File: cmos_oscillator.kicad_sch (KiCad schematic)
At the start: 5 parts, among them X1 YC24.576MUBCE2O

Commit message: Fixed a lot more mistakes...
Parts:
- X1: value YC24.576MUBCE2O -> SG-8018CE 30.720000MHz TJHPA; Price (none) -> $0.81
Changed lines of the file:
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@@
 			)
 		)
-		(property "Value" "YC24.576MUBCE2O"
+		(property "Value" "SG-8018CE 30.720000MHz TJHPA"
 			(at 123.19 87.5598 0)
 			(hide yes)
@@
 			)
 		)
-		(property "Datasheet" "https://jlc-prod-smt.oss-eu-central-1.aliyuncs.com/smtDataManualFile/8588933966032617472-C390505.pdf?response-content-disposition=attachment%3B%20filename%3DC390505.pdf%3B%20filename%2A%3DUTF-8%27%27C390505.pdf&x-oss-date=20260713T192353Z&x-oss-expires=1800&x-oss-security-token=CAISgAN1q6Ft5B2yfSjIr5vDP9Dej5xk%2BpGdWEveplljb850orDClzz2IHhMdHJsAOodtv0%2FmmhT6PkclqRLcbhpcmfjV%2BZHzLB8qeYbqwhc4J7b16cNrbH4M4H6aXeirtuwDsz9SNTCALjPD3nPii50x5bjaDymRCbLGJaViJlhHLN1Ow6jdmhpCctxLAlvo9NgFxm3D%2Fu2NQPwiWf9FVdhvhEG6Vly8qOi2MaRmFy8yFTx0b0SvJ%2BjYMrmPctoN9JnSdC5mfdzau3a1TJ84gRD0a5wkaVA1zbDs5bfISEIuUzebreLqY03dV4mOvdqIcMe8qigz88fk%2FfIioH6xyxKOexoSCnFTOiiupCcQLPyao9jLu6iayqViY7QaIOTqQohZmkAMwVOasAsI3Ngh4zF97Qt0cVNkXO9gWfLI8DtuMleWhqAVs9ZwtHD0eS19jklBdzSlusJRAJJUVBflCeKEaRNSAd3WGhEfM2%2BBt4QT30w5N2u00S8OSMIzW17T6KWD5sagAEH0XQONBvK6BPLgnV8C207PLCKWk33RIXe%2FHW%2F%2BZhfMTLPa0UGk%2FYzlRC4zZHvrydpEGvZPRvOS0gXofU%2F2USkHG86fPOzGUhEgAFDSFwfe%2FrWC2%2FtY7pQNlxUNhLS%2BtO77iZMJH7wIZrwCswWjOwBqQYZ0YqcFTXTkg419%2FMEByAA&x-oss-signature-version=OSS4-HMAC-SHA256&x-oss-credential=STS.NXvtjjbCEMSvZmoBY6cAXMuiu%2F20260713%2Feu-central-1%2Foss%2Faliyun_v4_request&x-oss-signature=465519691e5ea808d0ae9e849a0f4727078b0ea6ca732cde5a2652c1c89228d5"
+		(property "Datasheet" "https://jlc-prod-smt.oss-eu-central-1.aliyuncs.com/smtDataManualFile/8588933966032617472-C390505.pdf?response-content-disposition=attachment%3B%20filename%3DC390505.pdf%3B%20filename%2A%3DUTF-8%27%27C390505.pdf&x-oss-date=20260722T003906Z&x-oss-expires=1800&x-oss-security-token=CAISgAN1q6Ft5B2yfSjIr5rHM%2B3smZ1Gx5CjaXPhtkIPXbwVnITJkTz2IHhMdHJsAOodtv0%2FmmhT6PkclqRLcbhpcmfjV%2BZHzLB8qeAV7l5R4J7b16cNrbH4M4H6aXeirtuwDsz9SNTCALjPD3nPii50x5bjaDymRCbLGJaViJlhHLN1Ow6jdmhpCctxLAlvo9NgFxm3D%2Fu2NQPwiWf9FVdhvhEG6Vly8qOi2MaRmFy8yFTx0b0SvJ%2BjYMrmPctoN9JnSdC5mfdzau3a1TJ84gRD0a5wkaVA1zbDs5bfISEIuUzebreLqY03dV4mOvdqIcMe8qigz88fk%2FfIioH6xyxKOexoSCnFTOiiupCcQLPyao9jLu6iayqViY7QaIOTqQohZmkAMwVOasAsI3Ngh4zF97Qt0cVNkXO9gWfLI8DtuMleWhpDE1NnmtHD0eS19jklBdzSlusJRAJJUVBflCeKEaRNSAd3WGhEfM2%2BBt4QT30w5N2u00S8OSMIMiDpfqKWD5sagAEIuex4%2FS4WddUM%2Fq31QMVuF1DjmKritBzmY7UsaeVXE5Y6cA2DIdCzyPbeZ7RXLbCbbvJ2w5S1gitzOQ2fpNn9WVrjqKde8H8UphDH%2FgQAWjP3Pk81SE5E2wJntjGHD%2B6K7yM2tP4pwvLZeXjm3G7dh4KBqQB8jh4W0%2FJBLiEqkiAA&x-oss-signature-version=OSS4-HMAC-SHA256&x-oss-credential=STS.NYrxWXtBgpRHkUPRBZQ39sAbs%2F20260722%2Feu-central-1%2Foss%2Faliyun_v4_request&x-oss-signature=a025f17aa42fdaad05dfb79b8c5d52c1bd33945fd76a011e5d9cb6ae45cacf93"
 			(at 107.95 91.44 0)
 			(hide yes)
@@
 			)
 		)
-		(property "Description" "SG-8018CE 30.720000MHz TJHPA"
+		(property "Description" "-40℃~+105℃ 1.8V~3.3V 30.72MHz ±50ppm SMD3225-4P Programmable Oscillators ROHS"
 			(at 110.49 91.44 0)
 			(hide yes)
@@
 			(at 110.49 91.44 0)
 			(hide yes)
+			(show_name no)
+			(do_not_autoplace no)
+			(effects
+				(font
+					(size 1.27 1.27)
+				)
+			)
+		)
+		(property "Price" "$0.81"
+			(at 110.49 91.44 0)
+			(hide yes)

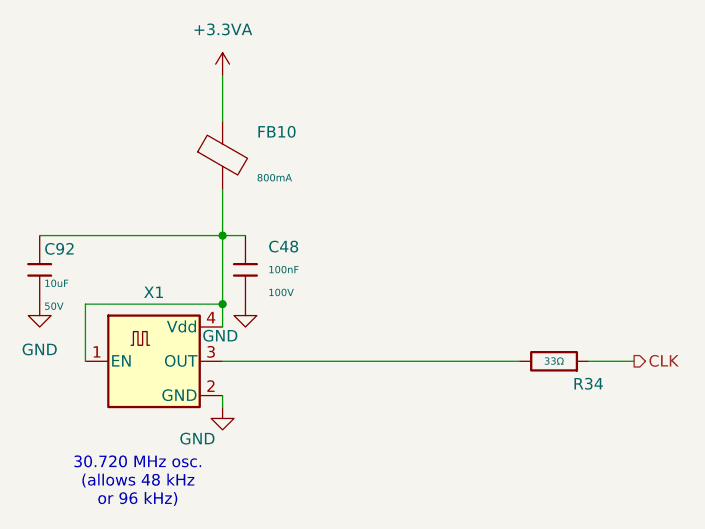
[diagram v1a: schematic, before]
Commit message: Starting to place components
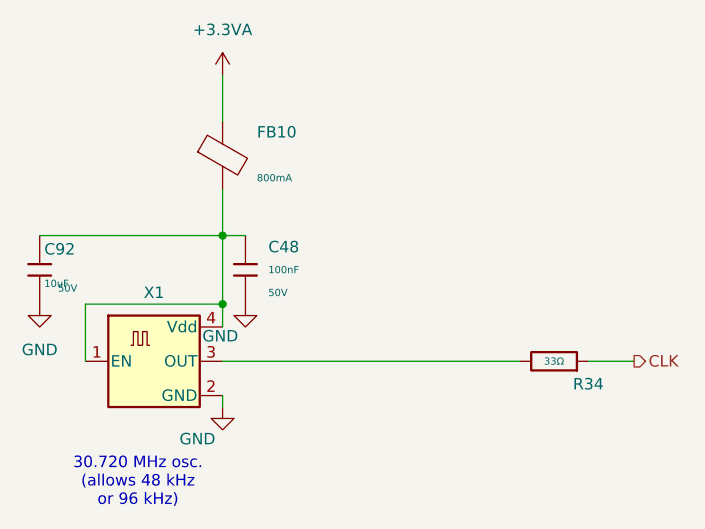
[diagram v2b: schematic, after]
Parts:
- C48: footprint PCM_JLCPCB:C_0805 -> PCM_JLCPCB:C_0402; symbol PCM_JLCPCB-Capacitors:0805,100nF -> PCM_JLCPCB-Capacitors:0402,100nF,(2); LCSC C28233 -> C307331; Manufacturer (none) -> Samsung Electro-Mechanics; Part CL21B104KCFNNNE -> CL05B104KB54PNC; Price 0.009USD -> 0.008USD; Stock 1168020 -> 8389599; Voltage Rated 100V -> 50V
- C92: footprint PCM_JLCPCB:C_1206 -> PCM_JLCPCB:C_0805; symbol PCM_JLCPCB-Capacitors:1206,10uF -> PCM_JLCPCB-Capacitors:0805,10uF,(2); LCSC C13585 -> C440198; Manufacturer (none) -> Murata Electronics; Part CL31A106KBHNNNE -> GRM21BR61H106KE43L; Price 0.035USD -> 0.066USD; Stock 3698334 -> 1422246
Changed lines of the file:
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@@
 	)
 	(symbol
-		(lib_id "PCM_JLCPCB-Capacitors:0805,100nF")
+		(lib_id "PCM_JLCPCB-Capacitors:0402,100nF,(2)")
 		(at 120.65 81.28 0)
 		(unit 1)
@@
 			)
 		)
-		(property "Footprint" "PCM_JLCPCB:C_0805"
+		(property "Footprint" "PCM_JLCPCB:C_0402"
 			(at 118.872 81.28 90)
 			(hide yes)
@@
 			)
 		)
-		(property "Datasheet" "https://www.lcsc.com/datasheet/lcsc_datasheet_2304140030_Samsung-Electro-Mechanics-CL21B104KCFNNNE_C28233.pdf"
-			(at 120.65 81.28 0)
-			(hide yes)
-			(show_name no)
-			(do_not_autoplace no)
-			(effects
-				(font
-					(size 1.27 1.27)
-				)
-			)
-		)
-		(property "Description" "100V 100nF X7R ±10% 0805 Multilayer Ceramic Capacitors MLCC - SMD/SMT ROHS"
-			(at 120.65 81.28 0)
-			(hide yes)
-			(show_name no)
-			(do_not_autoplace no)
-			(effects
-				(font
-					(size 1.27 1.27)
-				)
-			)
-		)
-		(property "LCSC" "C28233"
-			(at 120.65 81.28 0)
-			(hide yes)
-			(show_name no)
-			(do_not_autoplace no)
-			(effects
-				(font
-					(size 1.27 1.27)
-				)
-			)
-		)
-		(property "Stock" "1168020"
-			(at 120.65 81.28 0)
-			(hide yes)
-			(show_name no)
-			(do_not_autoplace no)
-			(effects
-				(font
-					(size 1.27 1.27)
-				)
-			)
-		)
-		(property "Price" "0.009USD"
+		(property "Datasheet" "https://www.lcsc.com/datasheet/lcsc_datasheet_2304140030_Samsung-Electro-Mechanics-CL05B104KB54PNC_C307331.pdf"
+			(at 120.65 81.28 0)
+			(hide yes)
+			(show_name no)
+			(do_not_autoplace no)
+			(effects
+				(font
+					(size 1.27 1.27)
+				)
+			)
+		)
+		(property "Description" "50V 100nF X7R ±10% 0402 Multilayer Ceramic Capacitors MLCC - SMD/SMT ROHS"
+			(at 120.65 81.28 0)
+			(hide yes)
+			(show_name no)
+			(do_not_autoplace no)
+			(effects
+				(font
+					(size 1.27 1.27)
+				)
+			)
+		)
+		(property "LCSC" "C307331"
+			(at 120.65 81.28 0)
+			(hide yes)
+			(show_name no)
+			(do_not_autoplace no)
+			(effects
+				(font
+					(size 1.27 1.27)
+				)
+			)
+		)
+		(property "Stock" "8389599"
+			(at 120.65 81.28 0)
+			(hide yes)
+			(show_name no)
+			(do_not_autoplace no)
+			(effects
+				(font
+					(size 1.27 1.27)
+				)
+			)
+		)
+		(property "Price" "0.008USD"
 			(at 120.65 81.28 0)
 			(hide yes)
@@
 			)
 		)
-		(property "Part" "CL21B104KCFNNNE"
-			(at 120.65 81.28 0)
-			(hide yes)
-			(show_name no)
-			(do_not_autoplace no)
-			(effects
-				(font
-					(size 1.27 1.27)
-				)
-			)
-		)
-		(property "Voltage Rated" "100V"
+		(property "Part" "CL05B104KB54PNC"
+			(at 120.65 81.28 0)
+			(hide yes)
+			(show_name no)
+			(do_not_autoplace no)
+			(effects
+				(font
+					(size 1.27 1.27)
+				)
+			)
+		)
+		(property "Voltage Rated" "50V"
 			(at 123.19 83.82 0)
 			(show_name no)
@@
 		)
 		(property "Temperature Coefficient" "X7R"
+			(at 120.65 81.28 0)
+			(hide yes)
+			(show_name no)
+			(do_not_autoplace no)
+			(effects
+				(font
+					(size 1.27 1.27)
+				)
+			)
+		)
+		(property "Manufacturer" "Samsung Electro-Mechanics"
 			(at 120.65 81.28 0)
 			(hide yes)
@@
 	)
 	(symbol
-		(lib_id "PCM_JLCPCB-Capacitors:1206,10uF")
+		(lib_id "PCM_JLCPCB-Capacitors:0805,10uF,(2)")
 		(at 97.79 81.28 0)
 		(unit 1)
@@
 			)
 		)
-		(property "Footprint" "PCM_JLCPCB:C_1206"
+		(property "Footprint" "PCM_JLCPCB:C_0805"
 			(at 96.012 81.28 90)
 			(hide yes)
@@
 			)
 		)
-		(property "Datasheet" "https://www.lcsc.com/datasheet/lcsc_datasheet_2304140030_Samsung-Electro-Mechanics-CL31A106KBHNNNE_C13585.pdf"
-			(at 97.79 81.28 0)
-			(hide yes)
-			(show_name no)
-			(do_not_autoplace no)
-			(effects
-				(font
-					(size 1.27 1.27)
-				)
-			)
-		)
-		(property "Description" "50V 10uF X5R ±10% 1206 Multilayer Ceramic Capacitors MLCC - SMD/SMT ROHS"
-			(at 97.79 81.28 0)
-			(hide yes)
-			(show_name no)
-			(do_not_autoplace no)
-			(effects
-				(font
-					(size 1.27 1.27)
-				)
-			)
-		)
-		(property "LCSC" "C13585"
-			(at 97.79 81.28 0)
-			(hide yes)
-			(show_name no)
-			(do_not_autoplace no)
-			(effects
-				(font
-					(size 1.27 1.27)
-				)
-			)
-		)
-		(property "Stock" "3698334"
-			(at 97.79 81.28 0)
-			(hide yes)
-			(show_name no)
-			(do_not_autoplace no)
-			(effects
-				(font
-					(size 1.27 1.27)
-				)
-			)
-		)
-		(property "Price" "0.035USD"
+		(property "Datasheet" "https://www.lcsc.com/datasheet/lcsc_datasheet_2411041759_Murata-Electronics-GRM21BR61H106KE43L_C440198.pdf"
+			(at 97.79 81.28 0)
+			(hide yes)
+			(show_name no)
+			(do_not_autoplace no)
+			(effects
+				(font
+					(size 1.27 1.27)
+				)
+			)
+		)
+		(property "Description" "50V 10uF X5R ±10% 0805 Multilayer Ceramic Capacitors MLCC - SMD/SMT ROHS"
+			(at 97.79 81.28 0)
+			(hide yes)
+			(show_name no)
+			(do_not_autoplace no)
+			(effects
+				(font
+					(size 1.27 1.27)
+				)
+			)
+		)
+		(property "LCSC" "C440198"
+			(at 97.79 81.28 0)
+			(hide yes)
+			(show_name no)
+			(do_not_autoplace no)
+			(effects
+				(font
+					(size 1.27 1.27)
+				)
+			)
+		)
+		(property "Stock" "1422246"
+			(at 97.79 81.28 0)
+			(hide yes)
+			(show_name no)
+			(do_not_autoplace no)
+			(effects
+				(font
+					(size 1.27 1.27)
+				)
+			)
+		)
+		(property "Price" "0.066USD"
 			(at 97.79 81.28 0)
 			(hide yes)
@@
 			)
 		)
-		(property "Part" "CL31A106KBHNNNE"
+		(property "Part" "GRM21BR61H106KE43L"
 			(at 97.79 81.28 0)
 			(hide yes)
@@
 		)
 		(property "Voltage Rated" "50V"
-			(at 98.298 85.344 0)
+			(at 99.822 83.3262 0)
 			(show_name no)
 			(do_not_autoplace no)
@@
 			(at 97.79 81.28 0)
 			(hide yes)
+			(show_name no)
+			(do_not_autoplace no)
+			(effects
+				(font
+					(size 1.27 1.27)
+				)
+			)
+		)
+		(property "Manufacturer" "Murata Electronics"
+			(at 97.79 81.28 0)
+			(hide yes)

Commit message: AF DAC Some VDDA Placed
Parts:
- renumbered C92 to C55, C48 to C56, FB10 to FB6, R34 to R48
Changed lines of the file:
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@@
 		(dnp no)
 		(fields_autoplaced yes)
-		(property "Reference" "C48"
+		(property "Reference" "C56"
 			(at 123.19 78.7399 0)
 			(show_name no)
@@
 			(project "DDC_SDR"
 				(path "/7dfef218-ca21-47b0-a8d3-67c7d55cb9d2/6eb9cc2e-d7cc-44e8-9eee-d468fc47f0ed"
-					(reference "C48")
+					(reference "C56")
 					(unit 1)
 				)
@@
 		(in_pos_files yes)
 		(dnp no)
-		(property "Reference" "#PWR081"
+		(property "Reference" "#PWR0106"
 			(at 118.11 102.87 0)
 			(hide yes)
@@
 			(project "DDC_SDR"
 				(path "/7dfef218-ca21-47b0-a8d3-67c7d55cb9d2/6eb9cc2e-d7cc-44e8-9eee-d468fc47f0ed"
-					(reference "#PWR081")
+					(reference "#PWR0106")
 					(unit 1)
 				)
@@
 		(in_pos_files yes)
 		(dnp no)
-		(property "Reference" "R34"
+		(property "Reference" "R48"
 			(at 158.75 93.98 90)
 			(show_name no)
@@
 			(project "DDC_SDR"
 				(path "/7dfef218-ca21-47b0-a8d3-67c7d55cb9d2/6eb9cc2e-d7cc-44e8-9eee-d468fc47f0ed"
-					(reference "R34")
+					(reference "R48")
 					(unit 1)
 				)
@@
 		(dnp no)
 		(fields_autoplaced yes)
-		(property "Reference" "#PWR021"
+		(property "Reference" "#PWR0105"
 			(at 118.11 63.5 0)
 			(hide yes)
@@
 			(project "DDC_SDR"
 				(path "/7dfef218-ca21-47b0-a8d3-67c7d55cb9d2/6eb9cc2e-d7cc-44e8-9eee-d468fc47f0ed"
-					(reference "#PWR021")
+					(reference "#PWR0105")
 					(unit 1)
 				)
@@
 		(in_pos_files yes)
 		(dnp no)
-		(property "Reference" "#PWR082"
+		(property "Reference" "#PWR0107"
 			(at 120.65 91.44 0)
 			(hide yes)
@@
 			(project "DDC_SDR"
 				(path "/7dfef218-ca21-47b0-a8d3-67c7d55cb9d2/6eb9cc2e-d7cc-44e8-9eee-d468fc47f0ed"
-					(reference "#PWR082")
+					(reference "#PWR0107")
 					(unit 1)
 				)
@@
 		(dnp no)
 		(fields_autoplaced yes)
-		(property "Reference" "FB10"
+		(property "Reference" "FB6"
 			(at 121.92 65.9891 0)
 			(show_name no)
@@
 			(project "DDC_SDR"
 				(path "/7dfef218-ca21-47b0-a8d3-67c7d55cb9d2/6eb9cc2e-d7cc-44e8-9eee-d468fc47f0ed"
-					(reference "FB10")
+					(reference "FB6")
 					(unit 1)
 				)
@@
 		(in_pos_files yes)
 		(dnp no)
-		(property "Reference" "C92"
+		(property "Reference" "C55"
 			(at 98.298 78.994 0)
 			(show_name no)
@@
 			(project "DDC_SDR"
 				(path "/7dfef218-ca21-47b0-a8d3-67c7d55cb9d2/6eb9cc2e-d7cc-44e8-9eee-d468fc47f0ed"
-					(reference "C92")
+					(reference "C55")
 					(unit 1)
 				)
@@
 		(dnp no)
 		(fields_autoplaced yes)
-		(property "Reference" "#PWR0154"
+		(property "Reference" "#PWR0104"
 			(at 97.79 91.44 0)
 			(hide yes)
@@
 			(project "DDC_SDR"
 				(path "/7dfef218-ca21-47b0-a8d3-67c7d55cb9d2/6eb9cc2e-d7cc-44e8-9eee-d468fc47f0ed"
-					(reference "#PWR0154")
+					(reference "#PWR0104")
 					(unit 1)
 				)

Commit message: Fixed schematic errors, all placed
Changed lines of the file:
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@@
 		(property "Value" "GND"
 			(at 117.856 88.646 0)
+			(hide yes)
 			(show_name no)
 			(do_not_autoplace no)

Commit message: Added test points
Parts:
- added TP16: U15, TestPoint:TestPoint_THTPad_D2.5mm_Drill1.2mm, symbol Connector:TestPoint
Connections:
- net CLK: now also TP16.1
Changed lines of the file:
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@@
+	)
+	(junction
+		(at 161.29 91.44)
+		(diameter 0)
+		(color 0 0 0 0)
 	)
 	(junction
@@
 	(wire
 		(pts
+			(xy 161.29 91.44) (xy 163.83 91.44)
+		)
+		(stroke
+			(width 0)
+			(type default)
+		)
+	)
+	(wire
+		(pts
 			(xy 118.11 85.09) (xy 118.11 87.63)
 		)
@@
 	(wire
 		(pts
-			(xy 158.75 91.44) (xy 163.83 91.44)
+			(xy 158.75 91.44) (xy 161.29 91.44)
 		)
 		(stroke
@@
 					(unit 1)
 				)
+			)
+		)
+	)
+	(symbol
+		(lib_id "Connector:TestPoint")
+		(at 161.29 91.44 0)
+		(unit 1)
+		(body_style 1)
+		(exclude_from_sim no)
+		(in_bom yes)
+		(on_board yes)
+		(in_pos_files yes)
+		(dnp no)
+		(property "Reference" "TP16"
+			(at 161.29 85.09 90)
+			(hide yes)
+			(show_name no)
+			(do_not_autoplace no)
+			(effects
+				(font
+					(size 1.27 1.27)
+				)
+				(justify left)
+			)
+		)
+		(property "Value" "U15"
+			(at 162.56 87.376 0)
+			(show_name no)
+			(do_not_autoplace no)
+			(effects
+				(font
+					(size 1.27 1.27)
+				)
+				(justify left)
+			)
+		)
+		(property "Footprint" "TestPoint:TestPoint_THTPad_D2.5mm_Drill1.2mm"
+			(at 166.37 91.44 0)
+			(hide yes)
+			(show_name no)
+			(do_not_autoplace no)
+			(effects
+				(font
+					(size 1.27 1.27)
+				)
+			)
+		)
+		(property "Datasheet" ""
+			(at 166.37 91.44 0)
+			(hide yes)
+			(show_name no)
+			(do_not_autoplace no)
+			(effects
+				(font
+					(size 1.27 1.27)
+				)
+			)
+		)
+		(property "Description" ""
+			(at 161.29 91.44 0)
+			(hide yes)
+			(show_name no)
+			(do_not_autoplace no)
+			(effects
+				(font
+					(size 1.27 1.27)
+				)
+			)
+		)
+		(property "JLCPCB #" ""
+			(at 161.29 91.44 0)
+			(hide yes)
+			(show_name no)
+			(do_not_autoplace no)
+			(effects
+				(font
+					(size 1.27 1.27)
+				)
+			)
+		)
+		(pin "1"
+		)
+		(instances
+			(project "DDC_SDR"
+				(path "/7dfef218-ca21-47b0-a8d3-67c7d55cb9d2/6eb9cc2e-d7cc-44e8-9eee-d468fc47f0ed"
+					(reference "TP16")
+					(unit 1)
+				)

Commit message: Added Prototype Area
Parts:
- TP16: footprint TestPoint:TestPoint_THTPad_D2.5mm_Drill1.2mm -> RP2040_minimal:TestPoint_THTPad_D2.5mm_Drill1.2mm
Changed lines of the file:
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@@
 			)
 		)
-		(property "Footprint" "TestPoint:TestPoint_THTPad_D2.5mm_Drill1.2mm"
+		(property "Footprint" "RP2040_minimal:TestPoint_THTPad_D2.5mm_Drill1.2mm"
 			(at 166.37 91.44 0)
 			(hide yes)
